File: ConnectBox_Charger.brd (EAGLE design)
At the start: 65 x 30 mm, 12 parts, among them IC1 M24C32-RDW6TP, J1 CONNECTOR_PI_40_PIN, J2 Lithium Cell, J3 microUSB Power In, J4 FTDI Serial, J5 5V Charger Output, U1 LTC4040

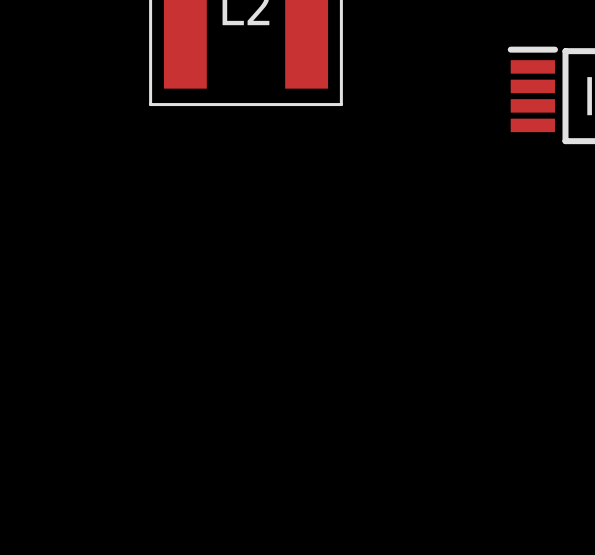
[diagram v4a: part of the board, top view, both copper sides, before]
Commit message: Start connecting LTC4040 charge control IC.
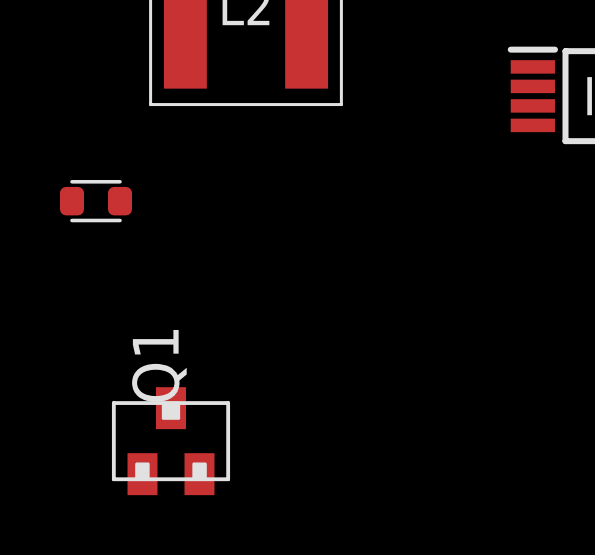
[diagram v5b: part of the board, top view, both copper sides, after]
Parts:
- added Q1: BSS138, APU_ENGR480_UPS_EAGLE_Library:BSS138
- added R4: 0.006R, ConnectBox_2019:RESC1608X55L25N
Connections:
- new net IGATE: Q1.G, U1.15
- new net N$2: Q1.S, R4.2, U1.7
- net +5V: now also Q1.D, U1.1
- net GND: now also U1.4, U1.5
- net V_IN: now also R4.1, U1.6
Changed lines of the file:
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@@
 <attribute name="VALUE" x="-59" y="-64.5" size="1.27" layer="27" align="center"/>
+</element>
+<element name="R4" library="ConnectBox_2019" package="RESC1608X55L25N" value="0.006R" x="-64" y="-71" smashed="yes">
+<attribute name="NAME" x="-62.222" y="-71" size="1.524" layer="25" font="vector" ratio="10" align="center"/>
+<attribute name="NAME" x="-64" y="-71" size="1.016" layer="51" ratio="10" align="center"/>
+</element>
+<element name="Q1" library="APU_ENGR480_UPS_EAGLE_Library" package="BSS138" value="BSS138" x="-61.5" y="-79" smashed="yes">
+<attribute name="AVAILABILITY" value="Good" x="-61.5" y="-79" size="1.778" layer="27" display="off"/>
+<attribute name="DESCRIPTION" value="B138 Series 50 V 6 Ohms N-Ch Logic Level Enhancement Mode FET - SOT-23-3" x="-61.5" y="-79" size="1.778" layer="27" display="off"/>
+<attribute name="MF" value="Fairchild Semiconductor" x="-61.5" y="-79" size="1.778" layer="27" display="off"/>
+<attribute name="MP" value="BSS138" x="-61.5" y="-79" size="1.778" layer="27" display="off"/>
+<attribute name="NAME" x="-61.5" y="-79" size="1.778" layer="51" ratio="10" align="center"/>
+<attribute name="NAME" x="-62.008" y="-76.46" size="1.524" layer="25" font="vector" ratio="10" rot="R90" align="center"/>
+<attribute name="PACKAGE" value="SOT-23-3 Fairchild Semiconductor" x="-61.5" y="-79" size="1.778" layer="27" display="off"/>
+<attribute name="PRICE" value="19.46 USD" x="-61.5" y="-79" size="1.778" layer="27" display="off"/>
 </element>
 </elements>
@@
 <contactref element="R1" pad="1"/>
 <contactref element="U1" pad="25"/>
+<contactref element="U1" pad="5"/>
+<contactref element="U1" pad="4"/>
 <wire x1="-44.8" y1="-61" x2="-44.8" y2="-64" width="0" layer="19" extent="1-1"/>
 <wire x1="-44.8" y1="-58" x2="-44.8" y2="-61" width="0" layer="19" extent="1-1"/>
@@
 <wire x1="-16.2" y1="-22.325" x2="-12" y2="-31" width="0" layer="19" extent="1-1"/>
 <wire x1="-20.5" y1="-12" x2="-16.2" y2="-22.325" width="0" layer="19" extent="1-1"/>
-<wire x1="-20.5" y1="-0.5" x2="-20.5" y2="-12" width="0" layer="19" extent="1-1"/>
+<wire x1="-22.435" y1="-1" x2="-20.5" y2="-12" width="0" layer="19" extent="1-1"/>
+<wire x1="-22.435" y1="-0.5" x2="-22.435" y2="-1" width="0" layer="19" extent="1-1"/>
+<wire x1="-20.5" y1="-0.5" x2="-22.435" y2="-0.5" width="0" layer="19" extent="1-1"/>
 </signal>
 <signal name="TO_PI">
@@
 <signal name="V_IN">
 <contactref element="J3" pad="1"/>
+<contactref element="U1" pad="6"/>
+<contactref element="R4" pad="1"/>
+<wire x1="-18.8" y1="-22.325" x2="-64.8" y2="-71" width="0" layer="19" extent="1-1"/>
+<wire x1="-22.435" y1="-1.5" x2="-18.8" y2="-22.325" width="0" layer="19" extent="1-1"/>
 </signal>
 <signal name="+5V">
@@
 <contactref element="S1" pad="5"/>
 <contactref element="S1" pad="6"/>
+<contactref element="Q1" pad="D"/>
+<contactref element="U1" pad="1"/>
+<wire x1="-42.27" y1="-46.2" x2="-61.5" y2="-77.9" width="0" layer="19" extent="1-1"/>
 <wire x1="-39.73" y1="-46.2" x2="-42.27" y2="-46.2" width="0" layer="19" extent="1-1"/>
 <wire x1="-37.19" y1="-46.2" x2="-39.73" y2="-46.2" width="0" layer="19" extent="1-1"/>
 <wire x1="-19" y1="-31" x2="-37.19" y2="-46.2" width="0" layer="19" extent="1-1"/>
-<wire x1="-21.5" y1="1.935" x2="-19" y2="-31" width="0" layer="19" extent="1-1"/>
+<wire x1="-22.435" y1="1" x2="-19" y2="-31" width="0" layer="19" extent="1-1"/>
+<wire x1="-21.5" y1="1.935" x2="-22.435" y2="1" width="0" layer="19" extent="1-1"/>
 <wire x1="8.37" y1="27.77" x2="-21.5" y2="1.935" width="0" layer="19" extent="1-1"/>
 <wire x1="10.91" y1="27.77" x2="8.37" y2="27.77" width="0" layer="19" extent="1-1"/>
@@
 <wire x1="-39.73" y1="-54.8" x2="-43.2" y2="-64" width="0" layer="19" extent="1-1"/>
 </signal>
+<signal name="N$2">
+<contactref element="R4" pad="2"/>
+<contactref element="U1" pad="7"/>
+<contactref element="Q1" pad="S"/>
+<wire x1="-63.2" y1="-71" x2="-60.55" y2="-80.1" width="0" layer="19" extent="1-1"/>
+<wire x1="-22.435" y1="-2" x2="-63.2" y2="-71" width="0" layer="19" extent="1-1"/>
+</signal>
+<signal name="IGATE">
+<contactref element="U1" pad="15"/>
+<contactref element="Q1" pad="G"/>
+<wire x1="-18.565" y1="-1" x2="-62.45" y2="-80.1" width="0" layer="19" extent="1-1"/>
+</signal>
 </signals>

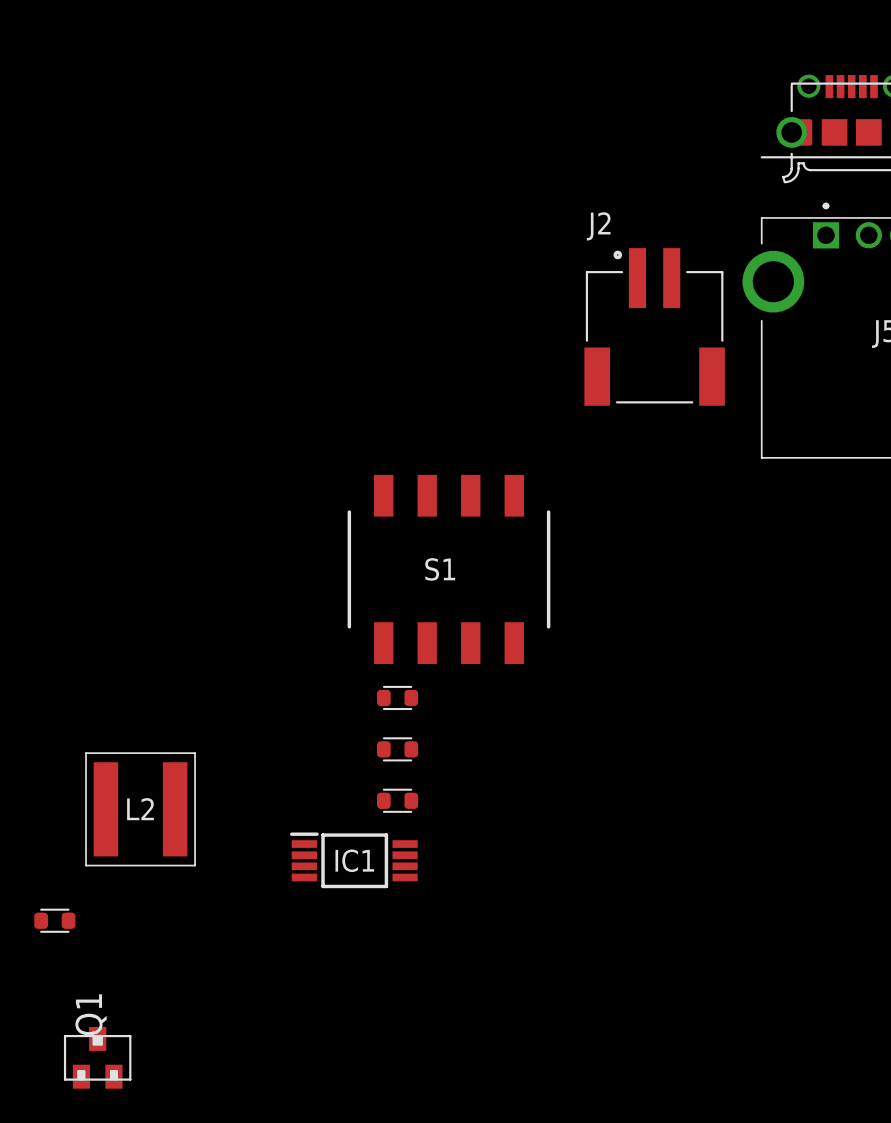
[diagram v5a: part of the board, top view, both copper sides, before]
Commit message: updated rotation on the LED  also replaced SSD card socket to a push push holder
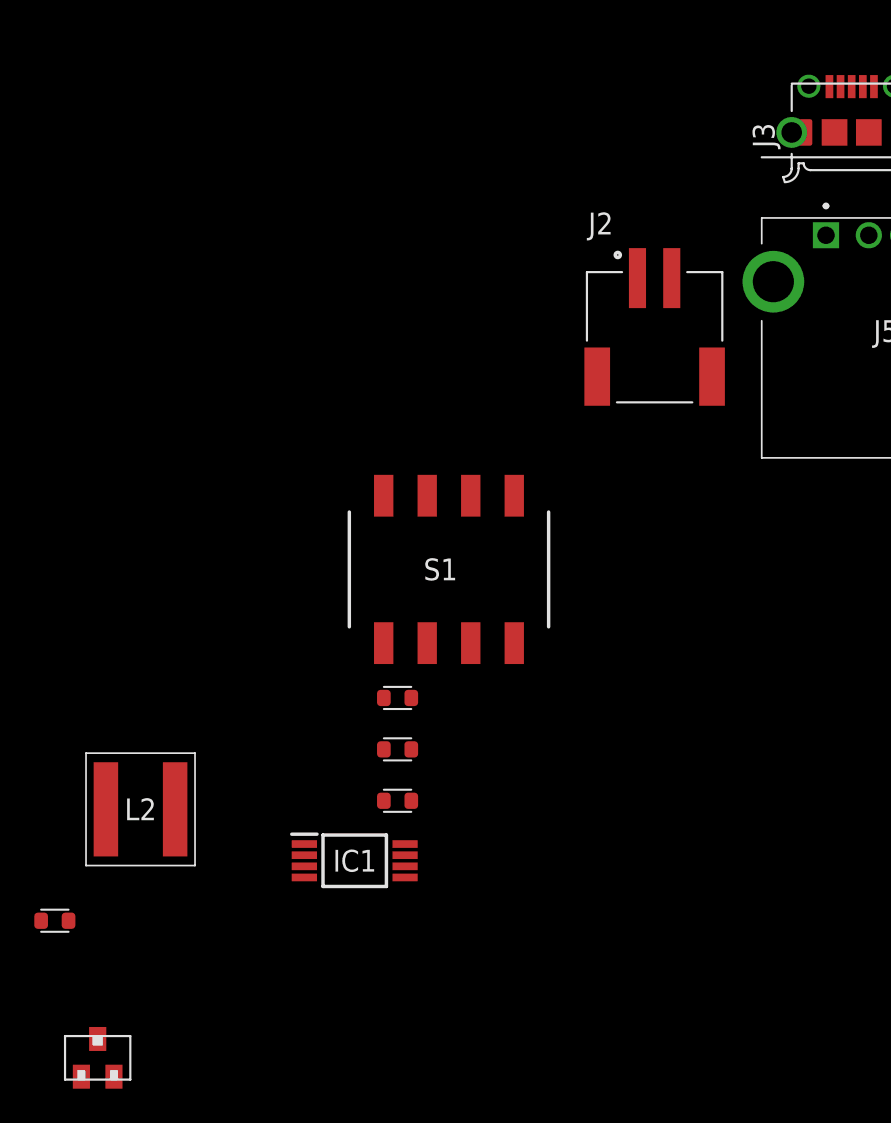
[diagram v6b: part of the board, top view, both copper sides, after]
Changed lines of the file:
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@@
 <?xml version="1.0" encoding="utf-8"?>
 <!DOCTYPE eagle SYSTEM "eagle.dtd">
-<eagle version="9.3.1">
+<eagle version="9.2.2">
 <drawing>
 <settings>
@@
 <attribute name="MF" value="FCI" x="-17.5" y="-25" size="1.778" layer="27" display="off"/>
 <attribute name="MP" value="10118194-0001LF" x="-17.5" y="-25" size="1.778" layer="27" display="off"/>
+<attribute name="NAME" x="-17.5" y="-24.365" size="2.54" layer="51" align="center"/>
 <attribute name="NAME" x="-22" y="-25.9" size="1.27" layer="25" rot="R90"/>
-<attribute name="NAME" x="-17.5" y="-24.365" size="2.54" layer="51" align="center"/>
 <attribute name="PACKAGE" value="DIP-4 FCI" x="-17.5" y="-25" size="1.778" layer="27" display="off"/>
 <attribute name="PRICE" value="0.24 USD" x="-17.5" y="-25" size="1.778" layer="27" display="off"/>
@@
 <attribute name="MF" value="Fairchild Semiconductor" x="-61.5" y="-79" size="1.778" layer="27" display="off"/>
 <attribute name="MP" value="BSS138" x="-61.5" y="-79" size="1.778" layer="27" display="off"/>
+<attribute name="NAME" x="-62.008" y="-76.46" size="1.524" layer="25" font="vector" ratio="10" rot="R90" align="center"/>
 <attribute name="NAME" x="-61.5" y="-79" size="1.778" layer="51" ratio="10" align="center"/>
-<attribute name="NAME" x="-62.008" y="-76.46" size="1.524" layer="25" font="vector" ratio="10" rot="R90" align="center"/>
 <attribute name="PACKAGE" value="SOT-23-3 Fairchild Semiconductor" x="-61.5" y="-79" size="1.778" layer="27" display="off"/>
 <attribute name="PRICE" value="19.46 USD" x="-61.5" y="-79" size="1.778" layer="27" display="off"/>
